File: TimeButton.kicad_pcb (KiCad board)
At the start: 2 copper layers, 31.9 x 40 mm, 27 parts, among them J1 USB_C_Receptacle_USB2.0_16P, J2 TagConnect, J3 Conn_01x05_Pin, J4 Conn_01x03_Pin, SW1 SW_Push, U1 PIC18F15Q41-I/SS, U2 FT231XS

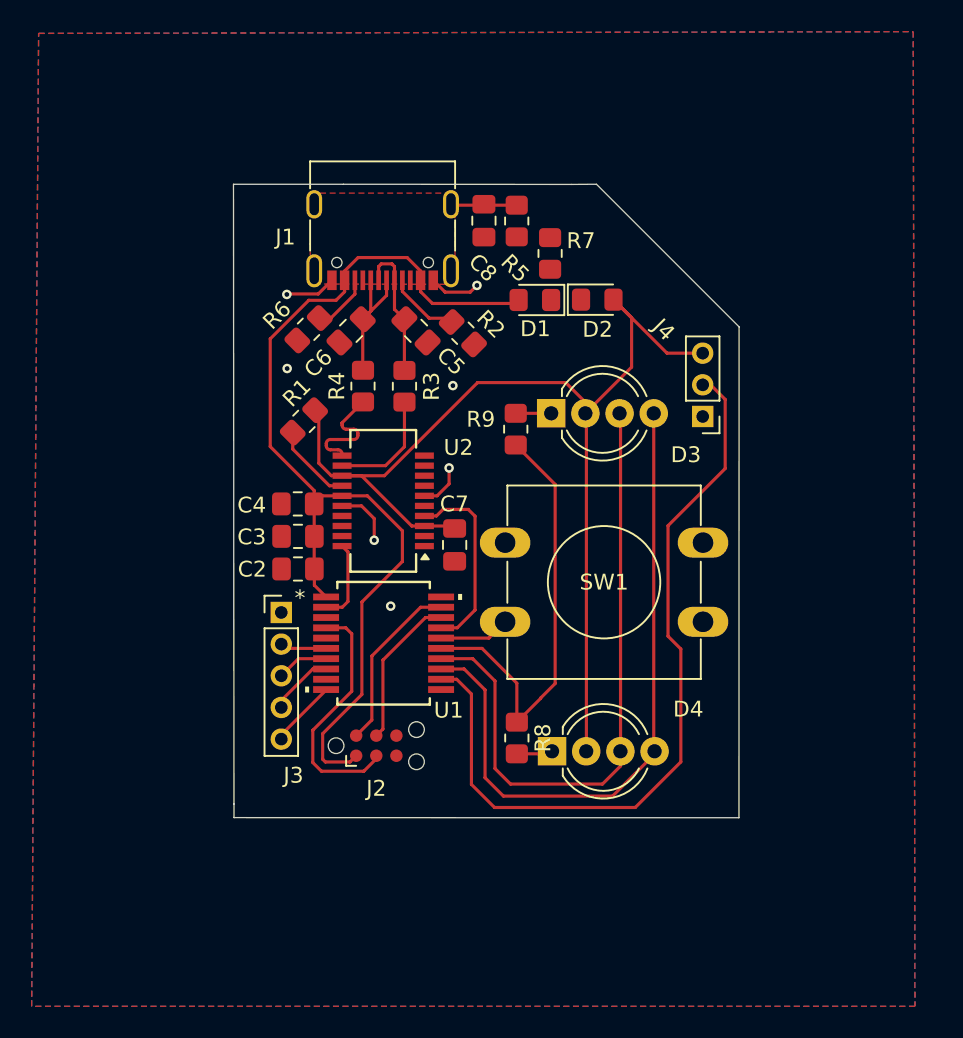
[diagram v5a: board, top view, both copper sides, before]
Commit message: Updated layout
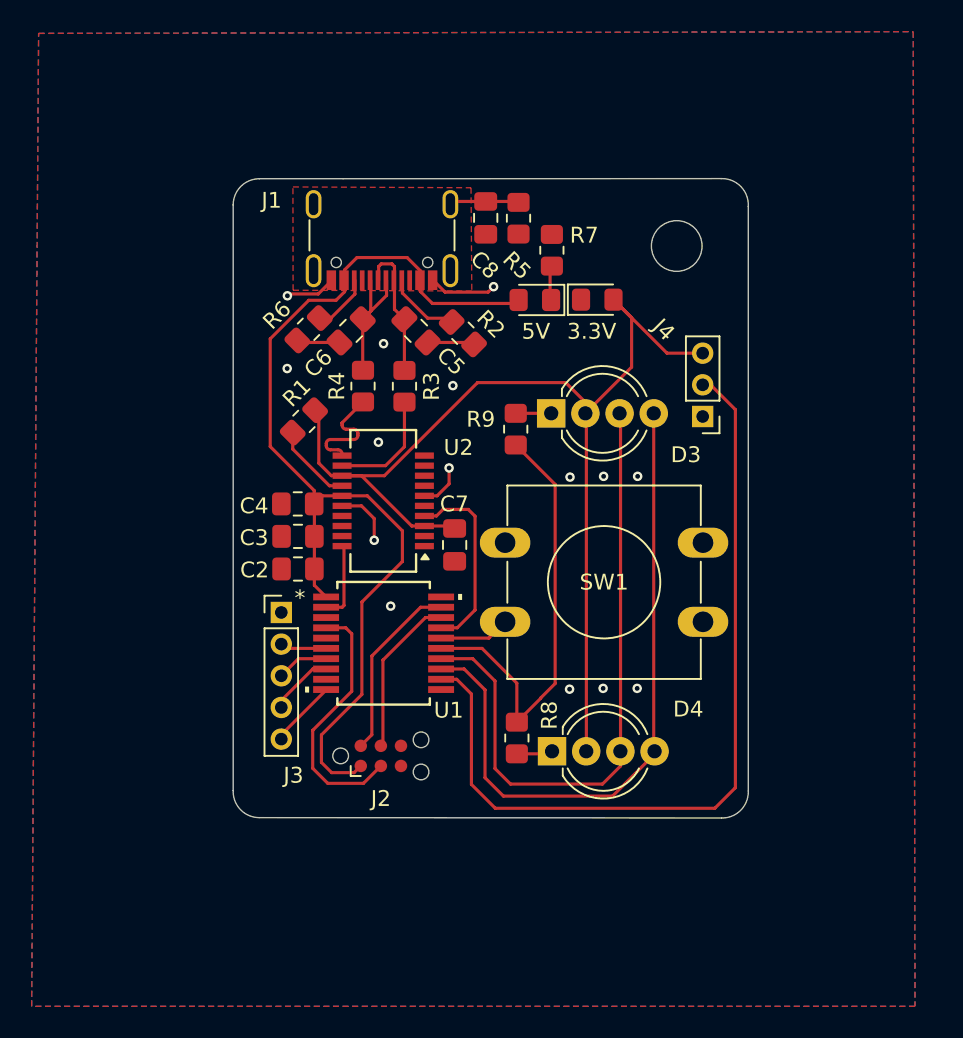
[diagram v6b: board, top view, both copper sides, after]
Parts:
- added REF**: MountingHole_3.2mm_M3_ISO14580, MountingHole:MountingHole_3.2mm_M3_ISO14580, F.Cu at (61.1, 31.9)
- moved J2 0.71 mm to (42.4, 64.1)
- moved R7 0.23 mm to (53.2, 32.1)
- moved R5 0.21 mm to (51.1, 30.1)
- moved C8 0.21 mm to (49.0, 30.1)
- renumbered D2 to 3.3V, D1 to 5V
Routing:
- net GND: track 13.1 -> 19.8 mm, vias 7 -> 15
- net Net-(J4-Pin_2): track 49.6 -> 52.4 mm
- net Net-(D1-K): track 0.00 -> 1.97 mm
- net 5V: track 64.0 -> 64.8 mm
- net nRST: track 15.7 -> 16.4 mm
- net SWDIO: track 11.1 -> 11.6 mm
- net SWCLK: track 9.73 -> 10.3 mm
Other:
- board size 31.9 x 40 mm -> 32.5 x 40.4 mm
